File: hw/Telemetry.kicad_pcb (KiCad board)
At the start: 4 copper layers, 100 x 82 mm, 121 parts, among them J102 BOOT0, J103 SPORT, J104 SBUS, J105 USB_B_Micro, J106 UART_EXP, J201 Conn_01x02, J301 Conn_01x02, J302 Conn_01x02, J401 Conn_01x02, J402 Conn_01x02, J403 Conn_01x02, J404 Conn_01x02, J405 Conn_01x02, J406 Conn_01x02, J407 Conn_01x02, J408 Conn_01x02, J409 SERVO_OUT, J410 AUDIO, Q201 AO3401A, Q202 AO3401A, Q203 IRLML6344TRPBF, Q204 IRLML6344TRPBF, Q401 IRLML6344TRPBF, Q402 IRLML6344TRPBF, Q403 IRLML6344TRPBF, Q404 CSD17306Q5A, Q405 IRLML6344TRPBF, Q406 IRLML6344TRPBF, Q407 IRLML6344TRPBF, Q408 CSD17306Q5A, SW101 SW_Push, U101 STM32F303CBx, U102 IS25LP032D, U201 AP1501-K5, U202 RT6200, U301 LP2985-5.0, U302 ACS770xCB-100U-PSF, U303 OP179GRT, U304 ACS770xCB-100U-PSF, U305 OP179GRT, U401 MCP1416, U402 MCP1416, U403 MCP4012-xxxxCH, U404 OP179GRT, X101 TXC-7C

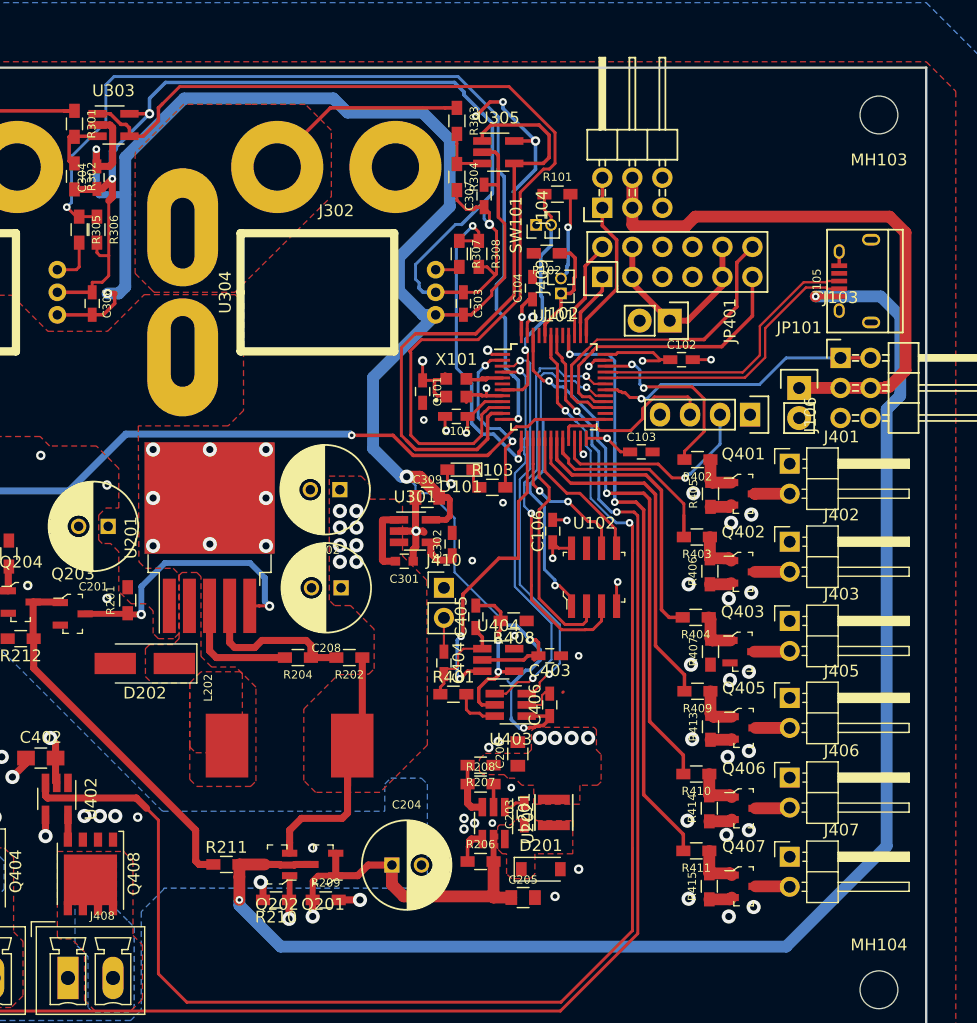
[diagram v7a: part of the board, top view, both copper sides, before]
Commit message: Added SWD connector for debugging
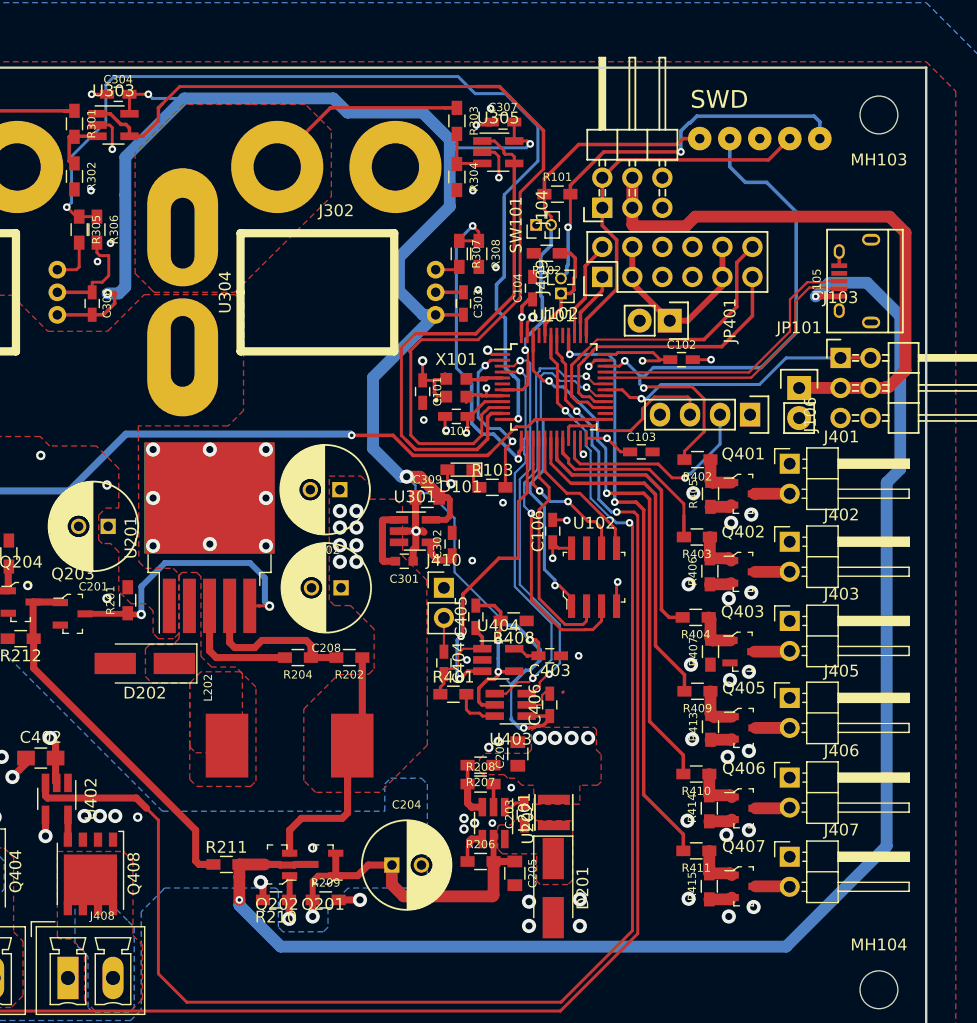
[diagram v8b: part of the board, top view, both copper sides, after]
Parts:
- added TP101: RST, Wire_Pads:SolderWirePad_single_0-8mmDrill, F.Cu at (140.8, 44.0)
- added TP102: SWDIO, Wire_Pads:SolderWirePad_single_0-8mmDrill, F.Cu at (143.4, 44.0)
- added TP103: SWCLK, Wire_Pads:SolderWirePad_single_0-8mmDrill, F.Cu at (148.5, 44.0)
- added TP104: 3V3, Wire_Pads:SolderWirePad_single_0-8mmDrill, F.Cu at (151.0, 44.0)
- added TP105: GND, Wire_Pads:SolderWirePad_single_0-8mmDrill, F.Cu at (145.9, 44.0)
- D201: footprint Diodes_SMD:D_SOD-123 -> Diodes_SMD:D_SMA_Handsoldering
- U303, U305, U404: value OP179GRT -> MCP6001-OT
- moved C304 7.28 mm to (91.7, 40.2), turned to 0 degrees
- moved C307 6.45 mm to (124.2, 42.6), turned to 0 degrees
- moved C205 2.17 mm to (125.2, 106.2), turned to 270 degrees
- moved D201 1.91 mm to (128.4, 107.4), turned to 270 degrees
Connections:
- R409 pad 2: OUT2 -> OUT4
- R410 pad 2: OUT4 -> OUT2
- U101 pad 18: OUT2 -> OUT4
- U101 pad 46: OUT4 -> OUT2
- U303 pad 2: +5VA -> GND
- U303 pad 5: GND -> +5VA
- U305 pad 2: +5VA -> GND
- U305 pad 5: GND -> +5VA
- U404 pad 2: +5VA -> GND
- U404 pad 5: GND -> +5VA
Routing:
- net GND: track 182.7 -> 90.0 mm, vias 78 -> 85
- net OUT1: track 16.2 -> 50.8 mm
- net +3V3: track 39.8 -> 66.7 mm, vias 13 -> 14
- net +5VA: track 169.4 -> 150.8 mm, vias 5 -> 6
- net /Sbus: track 15.4 -> 32.7 mm
- net Net-(R101-Pad1): track 20.2 -> 36.1 mm
- net OUT4: track 44.9 -> 29.7 mm, vias 2 -> 0
- net OUT2: track 29.7 -> 44.9 mm, vias 0 -> 2
- net ESC2_VOLTAGE_OUT: track 53.3 -> 45.3 mm
- net ESC1_CURRENT_OUT: track 77.7 -> 81.5 mm
- net ESC1_VOLTAGE_OUT: track 88.1 -> 86.5 mm
- net VBUS: track 124.4 -> 125.4 mm
- added copper zone on In2.Cu, net +BATT
- added copper zone on In2.Cu, net /Current measurement/ESC1_C_Negative
- added copper zone on In2.Cu, net /Current measurement/ESC2_C_Negative
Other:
- board text added: "SWD"
